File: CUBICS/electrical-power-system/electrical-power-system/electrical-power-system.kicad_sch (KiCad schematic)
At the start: 24 parts, among them J101 Conn_01x02, J102 Conn_01x02, J103 Conn_01x02, J104 Conn_01x02, J105 Conn_01x05, J106 Conn_01x05, J107 Conn_01x05, J108 Conn_01x05, J109 Conn_01x05, J110 Conn_01x05

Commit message: schematic v1.0
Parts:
- removed BT101, BT102, BT103, BT104: Battery_Cell, symbol Device:Battery_Cell
- removed J105, J106, J107, J108, J109, J110: Conn_01x05, symbol Connector_Generic:Conn_01x05
- added J101 (x4): Conn_01x05_Pin, Connector_Hirose:Hirose_DF13-05P-1.25DSA_1x05_P1.25mm_Vertical, symbol Connector:Conn_01x05_Pin
- added J105, J109: Conn_01x02, symbol Connector_Generic:Conn_01x02
- added J107, J108: Conn_02x26_Odd_Even, Connector_PinSocket_2.54mm:PinSocket_2x26_P2.54mm_Vertical, symbol Connector_Generic:Conn_02x26_Odd_Even
- added R501: 1.65k, symbol Device:R
- added U501: LTC4054XES5-4.2, Package_TO_SOT_SMD:TSOT-23-5, symbol Battery_Management:LTC4054XES5-4.2
- renumbered H103 to H102, H102 to H103
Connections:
- net +1V2: now also U501.4 (V_{CC})
- net +BATT: now also U501.3 (BAT); no longer J101.1 (Pin_1)
- net GND: now also J101.2 (Pin_2), J102.2 (Pin_2), J103.2 (Pin_2), J105.2 (Pin_2), J108.14 (Pin_14), J108.17 (Pin_17), J108.29 (Pin_29), J108.30 (Pin_30), J108.32 (Pin_32), J108.48 (Pin_48), J108.49 (Pin_49), J108.9 (Pin_9), J109.2 (Pin_2), R501.2, U501.2 (GND)
- net at D106.2 (A): now also J105.1 (Pin_1)
- net at D101.2 (A): now also J109.1 (Pin_1)
- net at D104.2 (A): now also J103.1 (Pin_1)
- net at D102.2 (A): now also J101.1 (Pin_1)
- net at J104.1 (Pin_1): now also D105.2 (A)
- net at J102.1 (Pin_1): now also D103.2 (A); no longer J101.2 (Pin_2)
- new net: R501.1, U501.5 (PROG)
- new net +3.3V: J101.5 (Pin_5), J101.5 (Pin_5), J101.5 (Pin_5), J101.5 (Pin_5), J108.27 (Pin_27), J108.28 (Pin_28)
- new net +5V: J107.47 (Pin_47), J107.49 (Pin_49), J108.25 (Pin_25), J108.26 (Pin_26)
- new net CANH: J107.42 (Pin_42)
- new net CANL: J107.44 (Pin_44)
- new net MISO_3V3: J101.2 (Pin_2), J101.2 (Pin_2), J101.2 (Pin_2), J101.2 (Pin_2)
- new net MOSI_3V3: J101.3 (Pin_3), J101.3 (Pin_3), J101.3 (Pin_3), J101.3 (Pin_3)
- new net SCK_3V3: J101.4 (Pin_4), J101.4 (Pin_4), J101.4 (Pin_4), J101.4 (Pin_4)
- new net SCL: J107.43 (Pin_43)
- new net SDA: J107.41 (Pin_41)
- new net ~{CS_PV1_3V3}: J101.1 (Pin_1)
- new net ~{CS_PV2_3V3}: J101.1 (Pin_1)
- new net ~{CS_PV3_3V3}: J101.1 (Pin_1)
- new net ~{CS_PV4_3V3}: J101.1 (Pin_1)
- no-connect marks 0 -> 87
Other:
- added sheet Buck Converters (buck_converters.kicad_sch)
- added sheet Cell (cell.kicad_sch)
- added sheet Cell1 (cell.kicad_sch)
- added sheet Cell2 (cell.kicad_sch)
- added sheet Cell3 (cell.kicad_sch)
- added sheet Inhibits (inhibits.kicad_sch)
- added sheet Micorcontroller (microcontroller.kicad_sch)
- note added: "4.5V - 6.5V Input"
- note added: "CHARGING LOGIC"
- note added: "CSKB HEADERS"
- note added: "H1"
- note added: "H2"
- note added: "PV POWER"
- note added: "SOLAR PANELS SPI INPUTS"
- moved on the sheet: D101, D102, D103, D104, D105, D106, H101, H102, H103, H104

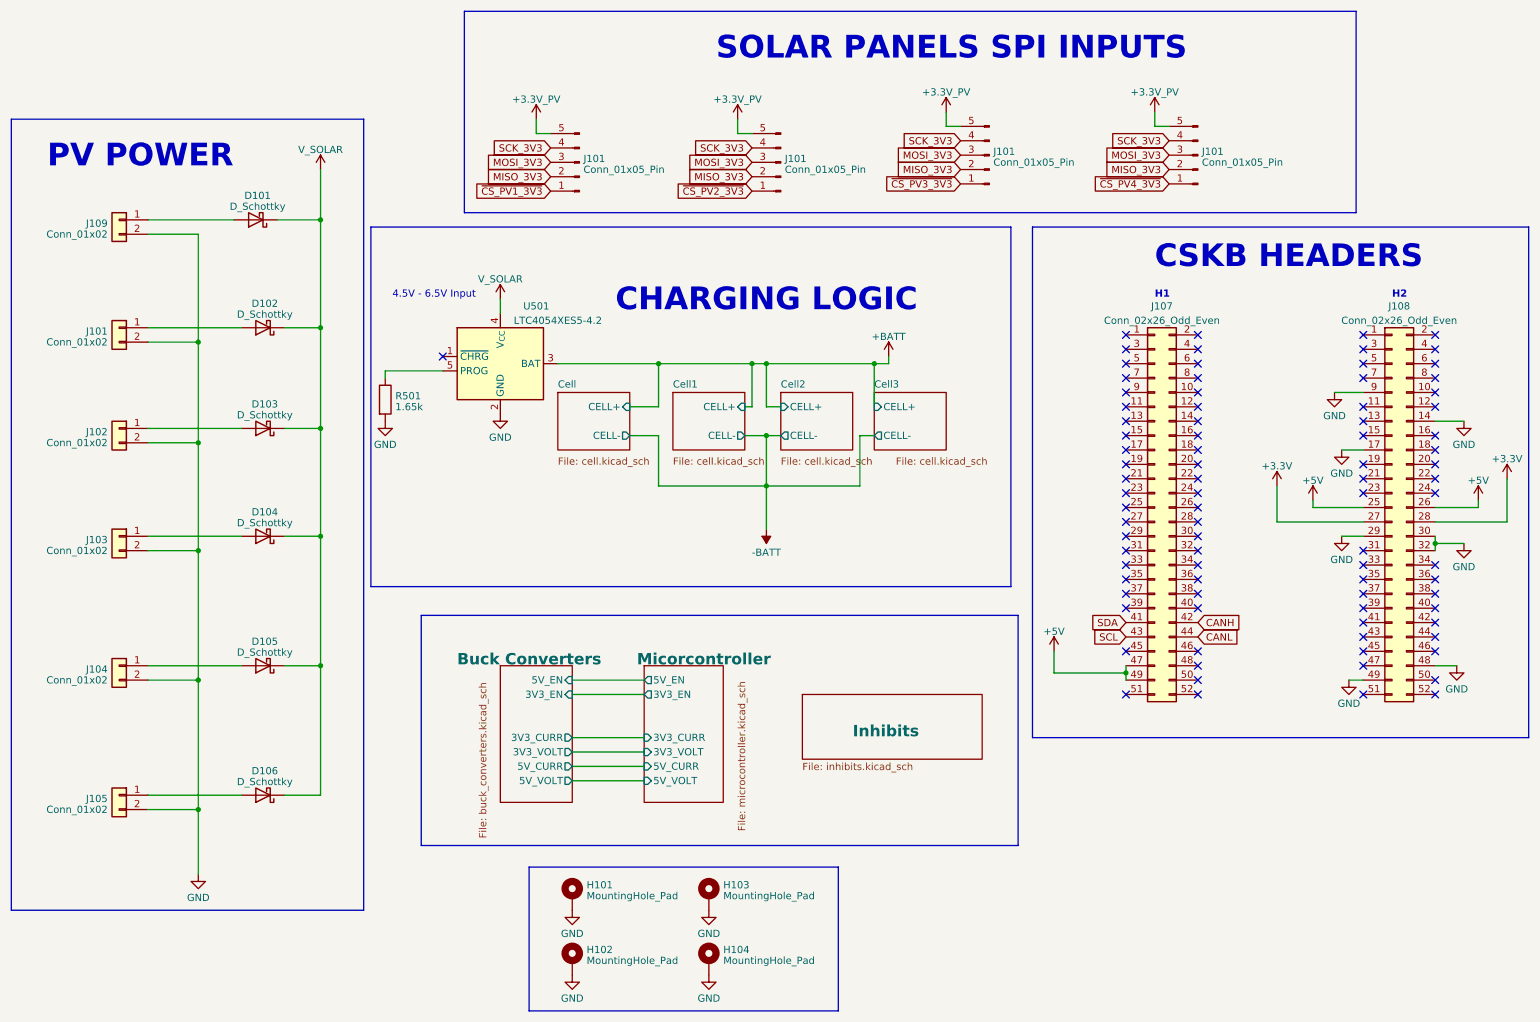
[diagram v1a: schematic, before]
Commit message: rev 1.0 routing complete updated schematic
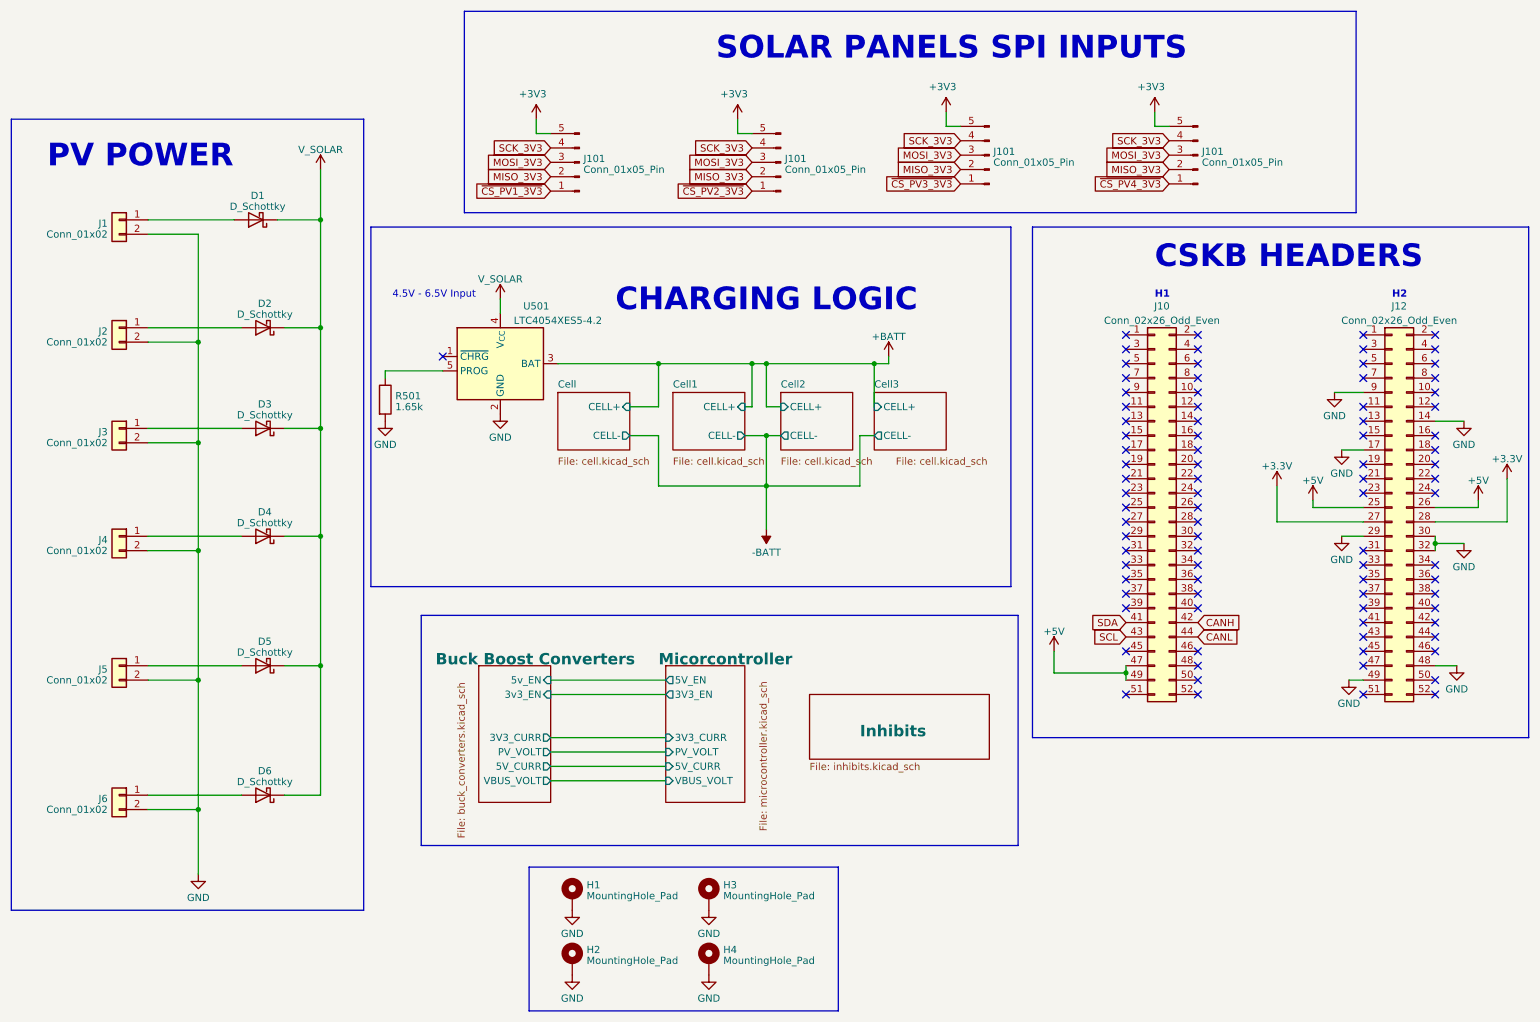
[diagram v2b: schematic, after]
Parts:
- D1: renamed from D101; footprint (none) -> Diode_THT:D_A-405_P10.16mm_Horizontal
- D2: renamed from D102; footprint (none) -> Diode_THT:D_A-405_P10.16mm_Horizontal
- D3: renamed from D103; footprint (none) -> Diode_THT:D_A-405_P10.16mm_Horizontal
- D4: renamed from D104; footprint (none) -> Diode_THT:D_A-405_P10.16mm_Horizontal
- D5: renamed from D105; footprint (none) -> Diode_THT:D_A-405_P10.16mm_Horizontal
- D6: renamed from D106; footprint (none) -> Diode_THT:D_A-405_P10.16mm_Horizontal
- H1: renamed from H101; footprint (none) -> MountingHole:MountingHole_3.2mm_M3_ISO7380_Pad_TopBottom
- H2: renamed from H102; footprint (none) -> MountingHole:MountingHole_3.2mm_M3_ISO7380_Pad_TopBottom
- H3: renamed from H103; footprint (none) -> MountingHole:MountingHole_3.2mm_M3_ISO7380_Pad_TopBottom
- H4: renamed from H104; footprint (none) -> MountingHole:MountingHole_3.2mm_M3_ISO7380_Pad_TopBottom
- J1: renamed from J109; footprint (none) -> Connector_PinHeader_2.54mm:PinHeader_1x02_P2.54mm_Vertical
- J2: renamed from J101; footprint (none) -> Connector_PinHeader_2.54mm:PinHeader_1x02_P2.54mm_Vertical
- J3: renamed from J102; footprint (none) -> Connector_PinHeader_2.54mm:PinHeader_1x02_P2.54mm_Vertical
- J4: renamed from J103; footprint (none) -> Connector_PinHeader_2.54mm:PinHeader_1x02_P2.54mm_Vertical
- J5: renamed from J104; footprint (none) -> Connector_PinHeader_2.54mm:PinHeader_1x02_P2.54mm_Vertical
- J6: renamed from J105; footprint (none) -> Connector_PinHeader_2.54mm:PinHeader_1x02_P2.54mm_Vertical
- R501: footprint (none) -> Resistor_SMD:R_0603_1608Metric
- renumbered J108 to J10, J107 to J12
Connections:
- net +3.3V: now also J12.27 (Pin_27), J12.28 (Pin_28); no longer J10.27 (Pin_27), J10.28 (Pin_28), J101.5 (Pin_5), J101.5 (Pin_5), J101.5 (Pin_5), J101.5 (Pin_5)
- net +5V: now also J10.47 (Pin_47), J10.49 (Pin_49), J12.25 (Pin_25), J12.26 (Pin_26); no longer J10.25 (Pin_25), J10.26 (Pin_26), J12.47 (Pin_47), J12.49 (Pin_49)
- net CANH: now also J10.42 (Pin_42); no longer J12.42 (Pin_42)
- net CANL: now also J10.44 (Pin_44); no longer J12.44 (Pin_44)
- net GND: now also J12.14 (Pin_14), J12.17 (Pin_17), J12.29 (Pin_29), J12.30 (Pin_30), J12.32 (Pin_32), J12.48 (Pin_48), J12.49 (Pin_49), J12.9 (Pin_9); no longer J10.14 (Pin_14), J10.17 (Pin_17), J10.29 (Pin_29), J10.30 (Pin_30), J10.32 (Pin_32), J10.48 (Pin_48), J10.49 (Pin_49), J10.9 (Pin_9)
- net SCL: now also J10.43 (Pin_43); no longer J12.43 (Pin_43)
- net SDA: now also J10.41 (Pin_41); no longer J12.41 (Pin_41)
- new net +3V3: J101.5 (Pin_5), J101.5 (Pin_5), J101.5 (Pin_5), J101.5 (Pin_5)
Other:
- sheet Buck Converters renamed Buck Boost Converters
- sheet Buck Boost Converters ports: added 3v3_EN, 5v_EN, PV_VOLT, VBUS_VOLT; removed 3V3_EN, 3V3_VOLT, 5V_EN, 5V_VOLT
- sheet Micorcontroller ports: added PV_VOLT, VBUS_VOLT; removed 3V3_VOLT, 5V_VOLT
- moved on the sheet: J10, J12
